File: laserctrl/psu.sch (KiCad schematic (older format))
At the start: 35 parts, among them P24 CONN_2, U7 MC34063, U8 78L05

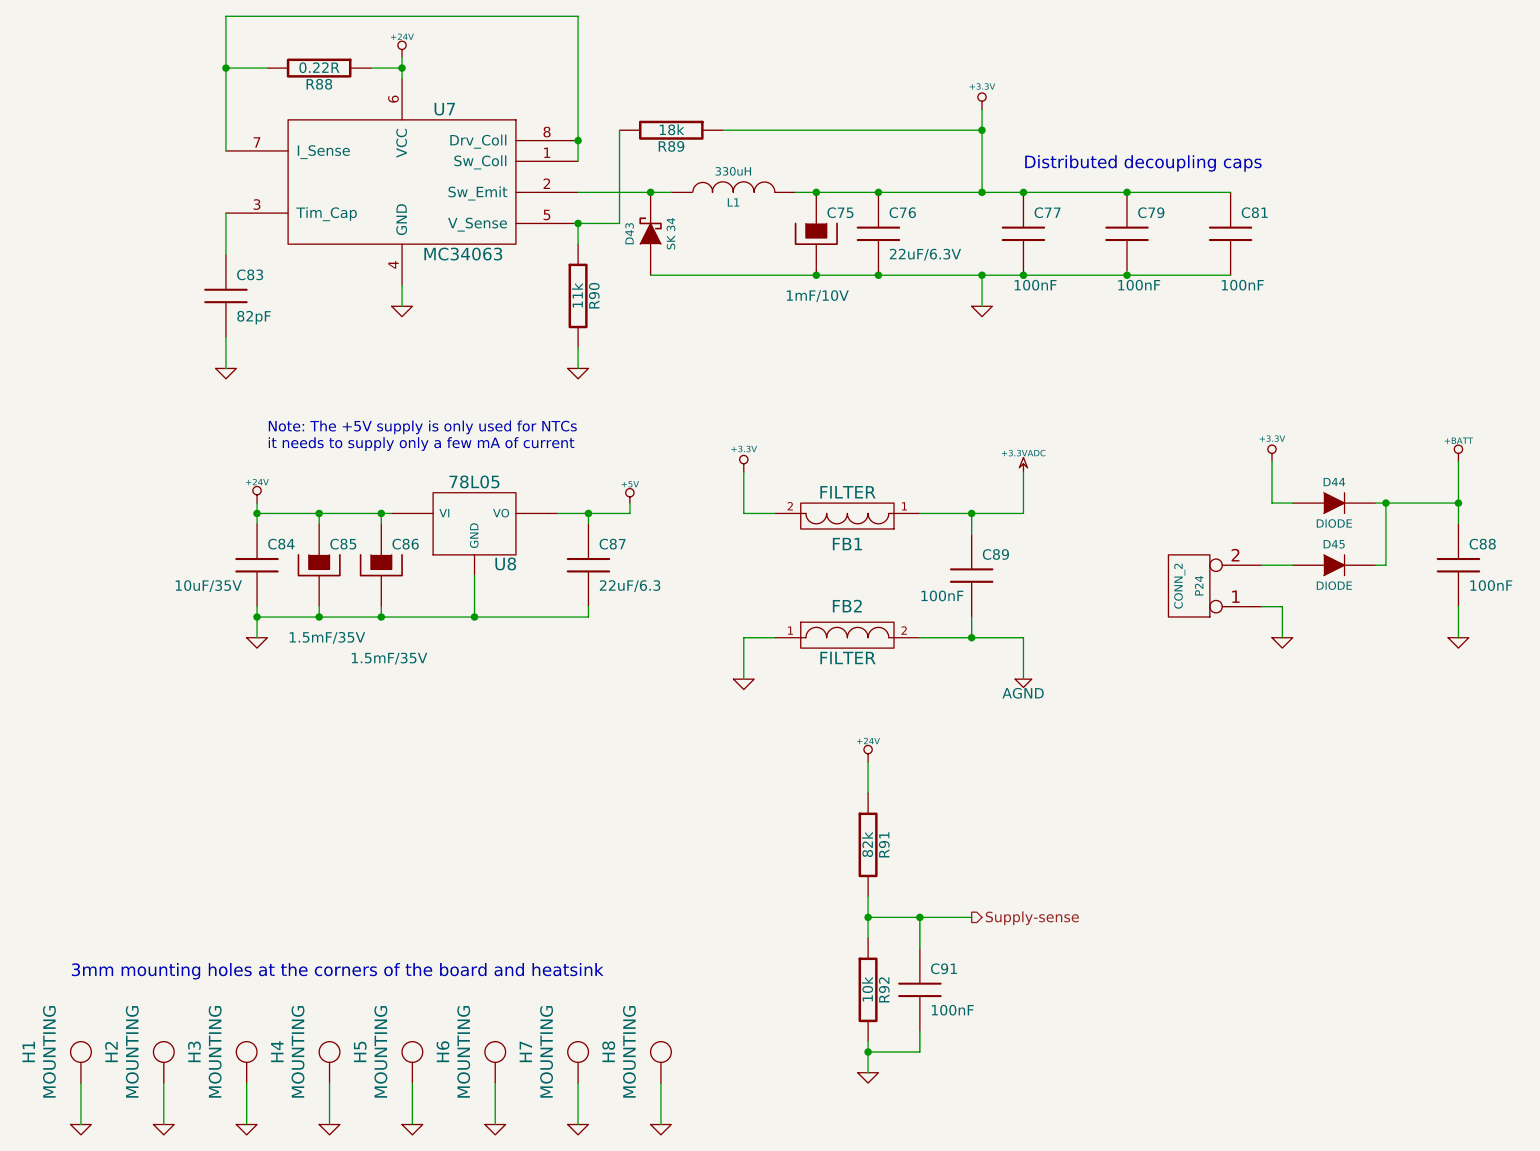
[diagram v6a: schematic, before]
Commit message: Use double-shottky diodes in stead of tons of discrete miniMELFs
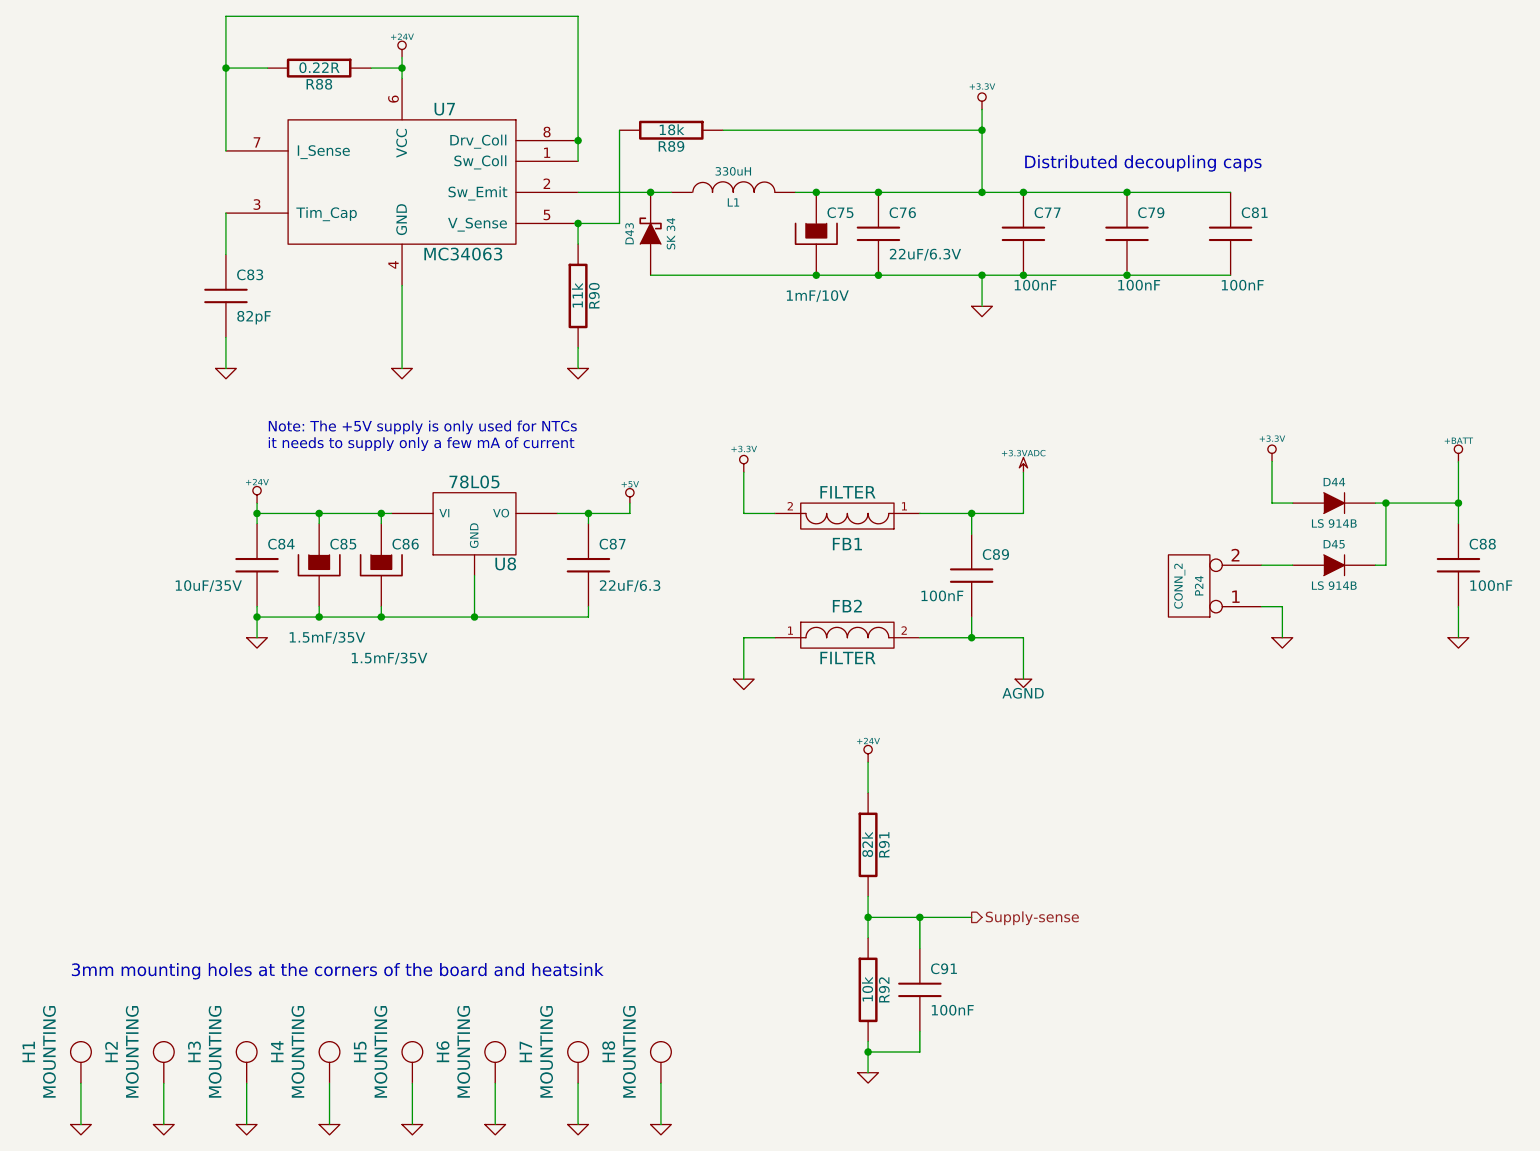
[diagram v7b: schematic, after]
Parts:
- D44, D45: value DIODE -> LS 914B
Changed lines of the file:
@@
-EESchema Schematic File Version 2  date 2011-11-09T19:37:00 CET
+EESchema Schematic File Version 2  date 2011-11-09T22:36:32 CET
 LIBS:power
 LIBS:device
@@
 LIBS:microsd
 LIBS:jumper3
+LIBS:diode2
+LIBS:laserctrl-cache
 EELAYER 25  0
 EELAYER END
@@
 	7050 3000 4250 3000
 Wire Wire Line
-	6050 4950 6050 4750
+	6050 4750 6050 4950
 Connection ~ 5550 6100
 Wire Wire Line
@@
 Connection ~ 3950 4150
 Wire Wire Line
-	4150 4100 4150 4150
-Wire Wire Line
-	4150 4150 3800 4150
+	4150 4150 4150 4100
+Wire Wire Line
+	3800 4150 4150 4150
 Connection ~ 3400 4650
 Wire Wire Line
-	3400 4450 3400 4650
+	3400 4650 3400 4450
 Connection ~ 2950 4650
 Wire Wire Line
-	2950 4600 2950 4650
+	2950 4650 2950 4600
 Connection ~ 2350 4150
 Wire Wire Line
-	2350 4150 3000 4150
+	3000 4150 2350 4150
 Connection ~ 2650 4650
 Wire Wire Line
@@
 Connection ~ 5800 4750
 Wire Wire Line
-	6050 4750 5550 4750
+	5550 4750 6050 4750
 Wire Wire Line
 	4850 4750 4700 4750
@@
 Connection ~ 5050 2600
 Wire Wire Line
-	5850 2300 4600 2300
+	4600 2300 5850 2300
 Connection ~ 4250 2600
 Wire Wire Line
@@
 	2200 2900 2200 2700
 Wire Wire Line
-	3050 3050 3050 3150
+	3050 3050 3050 3450
 Wire Wire Line
 	3900 2750 4100 2750
@@
 	3900 6900 3900 7100
 Wire Wire Line
-	5850 2200 5850 2600
+	5850 2600 5850 2200
 Connection ~ 6550 3000
 Wire Wire Line
@@
 $EndComp
 $Comp
-L +24V #PWR143
+L +24V #PWR0128
 U 1 1 4EB6CE24
 P 5300 5350
-F 0 "#PWR143" H 5300 5300 20  0001 C CNN
+F 0 "#PWR0128" H 5300 5300 20  0001 C CNN
 F 1 "+24V" H 5300 5450 30  0000 C CNN
 	1    5300 5350
@@
 $EndComp
 $Comp
-L GND #PWR144
+L GND #PWR0129
 U 1 1 4EB6CE1F
 P 5300 6850
-F 0 "#PWR144" H 5300 6850 30  0001 C CNN
+F 0 "#PWR0129" H 5300 6850 30  0001 C CNN
 F 1 "GND" H 5300 6780 30  0001 C CNN
 	1    5300 6850
@@
 Note: The +5V supply is only used for NTCs\nit needs to supply only a few mA of current
 $Comp
-L +5V #PWR137
+L +5V #PWR0130
 U 1 1 4EB54A98
 P 4150 4100
-F 0 "#PWR137" H 4150 4190 20  0001 C CNN
+F 0 "#PWR0130" H 4150 4190 20  0001 C CNN
 F 1 "+5V" H 4150 4190 30  0000 C CNN
 	1    4150 4100
@@
 $EndComp
 $Comp
-L GND #PWR138
+L GND #PWR0131
 U 1 1 4EB54922
 P 2350 4750
-F 0 "#PWR138" H 2350 4750 30  0001 C CNN
+F 0 "#PWR0131" H 2350 4750 30  0001 C CNN
 F 1 "GND" H 2350 4680 30  0001 C CNN
 	1    2350 4750
@@
 $EndComp
 $Comp
-L +24V #PWR136
+L +24V #PWR0132
 U 1 1 4EB5491D
 P 2350 4100
-F 0 "#PWR136" H 2350 4050 20  0001 C CNN
+F 0 "#PWR0132" H 2350 4050 20  0001 C CNN
 F 1 "+24V" H 2350 4200 30  0000 C CNN
 	1    2350 4100
@@
 $EndComp
 $Comp
-L AGND #PWR142
+L AGND #PWR0133
 U 1 1 4EB4727E
 P 6050 4950
-F 0 "#PWR142" H 6050 4950 40  0001 C CNN
+F 0 "#PWR0133" H 6050 4950 40  0001 C CNN
 F 1 "AGND" H 6050 4880 50  0000 C CNN
 	1    6050 4950
@@
 $EndComp
 $Comp
-L GND #PWR141
+L GND #PWR0134
 U 1 1 4EB4725D
 P 4700 4950
-F 0 "#PWR141" H 4700 4950 30  0001 C CNN
+F 0 "#PWR0134" H 4700 4950 30  0001 C CNN
 F 1 "GND" H 4700 4880 30  0001 C CNN
 	1    4700 4950
@@
 $EndComp
 $Comp
-L GND #PWR139
+L GND #PWR0135
 U 1 1 4EA3EFD9
 P 7300 4750
-F 0 "#PWR139" H 7300 4750 30  0001 C CNN
+F 0 "#PWR0135" H 7300 4750 30  0001 C CNN
 F 1 "GND" H 7300 4680 30  0001 C CNN
 	1    7300 4750
@@
 $EndComp
 $Comp
-L GND #PWR140
+L GND #PWR0136
 U 1 1 4EA3EF99
 P 8150 4750
-F 0 "#PWR140" H 8150 4750 30  0001 C CNN
+F 0 "#PWR0136" H 8150 4750 30  0001 C CNN
 F 1 "GND" H 8150 4680 30  0001 C CNN
 	1    8150 4750
@@
 $EndComp
 $Comp
-L +3.3V #PWR132
+L +3.3V #PWR0137
 U 1 1 4EA3EF91
 P 7250 3900
-F 0 "#PWR132" H 7250 3860 30  0001 C CNN
+F 0 "#PWR0137" H 7250 3860 30  0001 C CNN
 F 1 "+3.3V" H 7250 4010 30  0000 C CNN
 	1    7250 3900
@@
 $EndComp
 $Comp
-L +BATT #PWR133
+L +BATT #PWR0138
 U 1 1 4EA3EF72
 P 8150 3900
-F 0 "#PWR133" H 8150 3850 20  0001 C CNN
+F 0 "#PWR0138" H 8150 3850 20  0001 C CNN
 F 1 "+BATT" H 8150 4000 30  0000 C CNN
 	1    8150 3900
@@
 P 7550 4400
 F 0 "D45" H 7550 4500 40  0000 C CNN
-F 1 "DIODE" H 7550 4300 40  0000 C CNN
+F 1 "LS 914B" H 7550 4300 40  0000 C CNN
 	1    7550 4400
 	1    0    0    -1
@@
 P 7550 4100
 F 0 "D44" H 7550 4200 40  0000 C CNN
-F 1 "DIODE" H 7550 4000 40  0000 C CNN
+F 1 "LS 914B" H 7550 4000 40  0000 C CNN
 	1    7550 4100
 	1    0    0    -1
 $EndComp
 $Comp
-L +3.3VADC #PWR135
+L +3.3VADC #PWR0139
 U 1 1 4EA3E9DF
 P 6050 3950
-F 0 "#PWR135" H 6050 4070 20  0001 C CNN
+F 0 "#PWR0139" H 6050 4070 20  0001 C CNN
 F 1 "+3.3VADC" H 6050 4040 30  0000 C CNN
 	1    6050 3950
@@
 $EndComp
 $Comp
-L +3.3V #PWR134
+L +3.3V #PWR0140
 U 1 1 4EA3E96D
 P 4700 3950
-F 0 "#PWR134" H 4700 3910 30  0001 C CNN
+F 0 "#PWR0140" H 4700 3910 30  0001 C CNN
 F 1 "+3.3V" H 4700 4060 30  0000 C CNN
 	1    4700 3950
@@
 $EndComp
 $Comp
-L +3.3V #PWR127
+L +3.3V #PWR0141
 U 1 1 4EA3E60A
 P 5850 2200
-F 0 "#PWR127" H 5850 2160 30  0001 C CNN
+F 0 "#PWR0141" H 5850 2160 30  0001 C CNN
 F 1 "+3.3V" H 5850 2310 30  0000 C CNN
 	1    5850 2200
@@
 $EndComp
 $Comp
-L GND #PWR152
+L GND #PWR0142
 U 1 1 4EA1CE90
 P 4300 7100
-F 0 "#PWR152" H 4300 7100 30  0001 C CNN
+F 0 "#PWR0142" H 4300 7100 30  0001 C CNN
 F 1 "GND" H 4300 7030 30  0001 C CNN
 	1    4300 7100
@@
 $EndComp
 $Comp
-L GND #PWR151
+L GND #PWR0143
 U 1 1 4EA1CE88
 P 3900 7100
-F 0 "#PWR151" H 3900 7100 30  0001 C CNN
+F 0 "#PWR0143" H 3900 7100 30  0001 C CNN
 F 1 "GND" H 3900 7030 30  0001 C CNN
 	1    3900 7100
@@
 $EndComp
 $Comp
-L GND #PWR150
+L GND #PWR0144
 U 1 1 4EA1CE84
 P 3500 7100
-F 0 "#PWR150" H 3500 7100 30  0001 C CNN
+F 0 "#PWR0144" H 3500 7100 30  0001 C CNN
 F 1 "GND" H 3500 7030 30  0001 C CNN
 	1    3500 7100
@@
 $EndComp
 $Comp
-L GND #PWR149
+L GND #PWR0145
 U 1 1 4D879ADC
 P 3100 7100
-F 0 "#PWR149" H 3100 7100 30  0001 C CNN
+F 0 "#PWR0145" H 3100 7100 30  0001 C CNN
 F 1 "GND" H 3100 7030 30  0001 C CNN
 	1    3100 7100
@@
 3mm mounting holes at the corners of the board and heatsink
 $Comp
-L GND #PWR148
+L GND #PWR0146
 U 1 1 4D87999F
 P 2700 7100
-F 0 "#PWR148" H 2700 7100 30  0001 C CNN
+F 0 "#PWR0146" H 2700 7100 30  0001 C CNN
 F 1 "GND" H 2700 7030 30  0001 C CNN
 	1    2700 7100
@@
 $EndComp
 $Comp
-L GND #PWR147
+L GND #PWR0147
 U 1 1 4D87999A
 P 2300 7100
-F 0 "#PWR147" H 2300 7100 30  0001 C CNN
+F 0 "#PWR0147" H 2300 7100 30  0001 C CNN
 F 1 "GND" H 2300 7030 30  0001 C CNN
 	1    2300 7100
@@
 $EndComp
 $Comp
-L GND #PWR146
+L GND #PWR0148
 U 1 1 4D879997
 P 1900 7100
-F 0 "#PWR146" H 1900 7100 30  0001 C CNN
+F 0 "#PWR0148" H 1900 7100 30  0001 C CNN
 F 1 "GND" H 1900 7030 30  0001 C CNN
 	1    1900 7100
@@
 $EndComp
 $Comp
-L GND #PWR145
+L GND #PWR0149
 U 1 1 4D879990
 P 1500 7100
-F 0 "#PWR145" H 1500 7100 30  0001 C CNN
+F 0 "#PWR0149" H 1500 7100 30  0001 C CNN
 F 1 "GND" H 1500 7030 30  0001 C CNN
 	1    1500 7100
@@
 Distributed decoupling caps
 $Comp
-L GND #PWR129
+L GND #PWR0150
 U 1 1 4D04D42D
 P 5850 3150
-F 0 "#PWR129" H 5850 3150 30  0001 C CNN
+F 0 "#PWR0150" H 5850 3150 30  0001 C CNN
 F 1 "GND" H 5850 3080 30  0001 C CNN
 	1    5850 3150
@@
 $EndComp
 $Comp
-L GND #PWR130
+L GND #PWR0151
 U 1 1 4D04CF0D
 P 2200 3450
-F 0 "#PWR130" H 2200 3450 30  0001 C CNN
+F 0 "#PWR0151" H 2200 3450 30  0001 C CNN
 F 1 "GND" H 2200 3380 30  0001 C CNN
 	1    2200 3450
@@
 $EndComp
 $Comp
-L GND #PWR131
+L GND #PWR0152
 U 1 1 4D04CF06
 P 3900 3450
-F 0 "#PWR131" H 3900 3450 30  0001 C CNN
+F 0 "#PWR0152" H 3900 3450 30  0001 C CNN
 F 1 "GND" H 3900 3380 30  0001 C CNN
 	1    3900 3450
@@
 $EndComp
 $Comp
-L GND #PWR128
+L GND #PWR0153
 U 1 1 4D04CF02
-P 3050 3150
-F 0 "#PWR128" H 3050 3150 30  0001 C CNN
-F 1 "GND" H 3050 3080 30  0001 C CNN
-	1    3050 3150
+P 3050 3450
+F 0 "#PWR0153" H 3050 3450 30  0001 C CNN
+F 1 "GND" H 3050 3380 30  0001 C CNN
+	1    3050 3450
 	1    0    0    -1
 $EndComp
@@
 $EndComp
 $Comp
-L +24V #PWR126
+L +24V #PWR0154
 U 1 1 4D04CE42
 P 3050 1950
-F 0 "#PWR126" H 3050 1900 20  0001 C CNN
+F 0 "#PWR0154" H 3050 1900 20  0001 C CNN
 F 1 "+24V" H 3050 2050 30  0000 C CNN
 	1    3050 1950
